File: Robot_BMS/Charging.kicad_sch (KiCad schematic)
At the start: 33 parts, among them Q16 2N7002, Q17 2N7002, Q18 2N7002, U10 MCP73833-xxx-MF, U11 MCP73833-xxx-MF, U12 MCP73833-xxx-MF

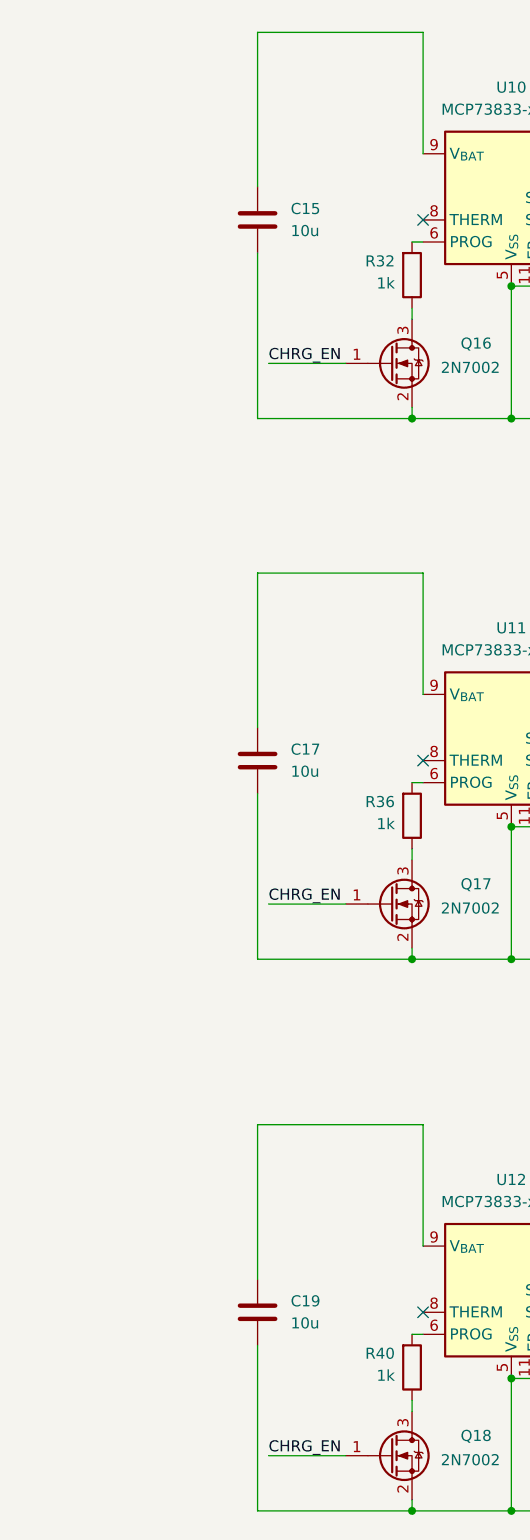
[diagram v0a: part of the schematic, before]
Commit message: cleaning up hierarchical schematics
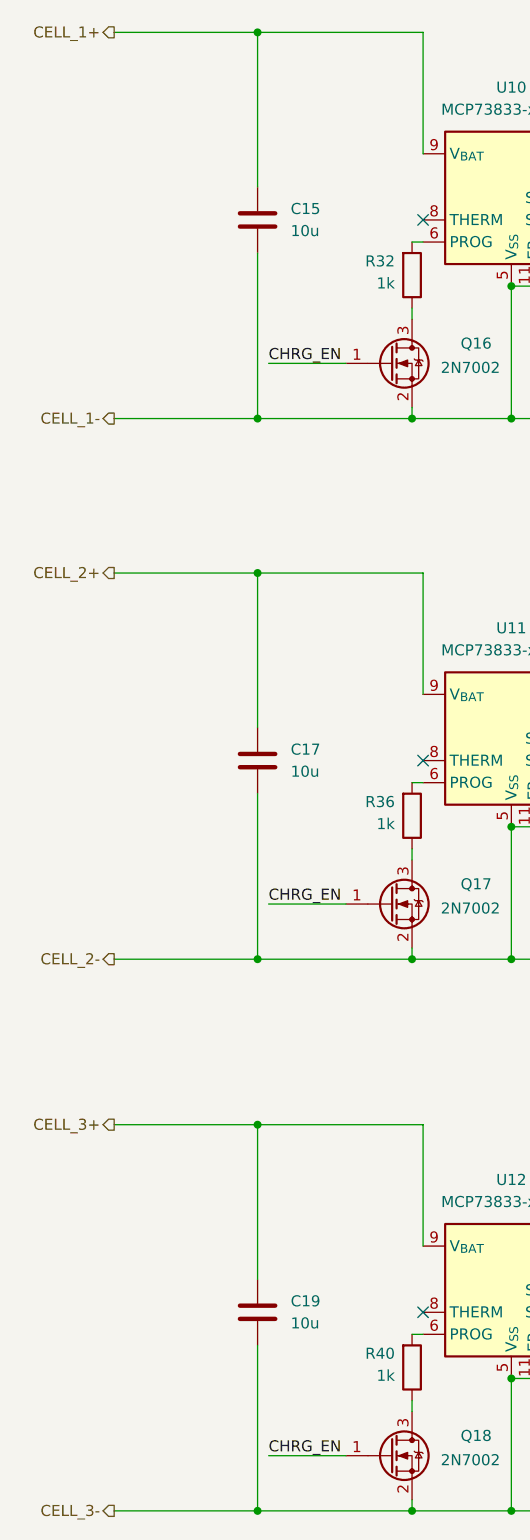
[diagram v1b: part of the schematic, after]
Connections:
- net CELL_2+: now reaches C17.1, U11.10 (V_{BAT}), U11.9 (V_{BAT})
- net CELL_2-: now reaches C17.2, C18.2, Q17.2 (S), U11.11 (EP), U11.5 (V_{SS})
- net CELL_3-: now reaches C19.2, C20.2, Q18.2 (S), U12.11 (EP), U12.5 (V_{SS})
- net CELL_3+: now reaches C19.1, U12.10 (V_{BAT}), U12.9 (V_{BAT})
- net CELL_1-: now reaches C15.2, C16.2, Q16.2 (S), U10.11 (EP), U10.5 (V_{SS})
- net CELL_1+: now reaches C15.1, U10.10 (V_{BAT}), U10.9 (V_{BAT})
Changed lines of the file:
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@@
+	)
+	(junction
+		(at 41.91 20.32)
+		(diameter 0)
+		(color 0 0 0 0)
+	)
+	(junction
+		(at 41.91 127)
+		(diameter 0)
+		(color 0 0 0 0)
 	)
 	(junction
@@
 	)
 	(junction
+		(at 41.91 64.77)
+		(diameter 0)
+		(color 0 0 0 0)
+	)
+	(junction
+		(at 41.91 146.05)
+		(diameter 0)
+		(color 0 0 0 0)
+	)
+	(junction
 		(at 153.67 19.05)
 		(diameter 0)
@@
 	)
 	(junction
+		(at 41.91 190.5)
+		(diameter 0)
+		(color 0 0 0 0)
+	)
+	(junction
 		(at 71.12 175.26)
 		(diameter 0)
@@
 	(junction
 		(at 153.67 144.78)
+		(diameter 0)
+		(color 0 0 0 0)
+	)
+	(junction
+		(at 41.91 82.55)
 		(diameter 0)
 		(color 0 0 0 0)
@@
 	(wire
 		(pts
+			(xy 25.4 127) (xy 41.91 127)
+		)
+		(stroke
+			(width 0)
+			(type default)
+		)
+	)
+	(wire
+		(pts
 			(xy 163.83 81.28) (xy 163.83 96.52)
 		)
@@
 	(wire
 		(pts
+			(xy 25.4 20.32) (xy 41.91 20.32)
+		)
+		(stroke
+			(width 0)
+			(type default)
+		)
+	)
+	(wire
+		(pts
 			(xy 115.57 34.29) (xy 153.67 34.29)
 		)
@@
 	(wire
 		(pts
+			(xy 25.4 64.77) (xy 41.91 64.77)
+		)
+		(stroke
+			(width 0)
+			(type default)
+		)
+	)
+	(wire
+		(pts
 			(xy 96.52 167.64) (xy 109.22 167.64)
 		)
@@
 	(wire
 		(pts
+			(xy 25.4 146.05) (xy 41.91 146.05)
+		)
+		(stroke
+			(width 0)
+			(type default)
+		)
+	)
+	(wire
+		(pts
 			(xy 99.06 49.53) (xy 115.57 49.53)
 		)
@@
 	(wire
 		(pts
+			(xy 25.4 82.55) (xy 41.91 82.55)
+		)
+		(stroke
+			(width 0)
+			(type default)
+		)
+	)
+	(wire
+		(pts
 			(xy 153.67 144.78) (xy 109.22 144.78)
 		)
@@
 		(pts
 			(xy 41.91 146.05) (xy 41.91 163.83)
+		)
+		(stroke
+			(width 0)
+			(type default)
+		)
+	)
+	(wire
+		(pts
+			(xy 25.4 190.5) (xy 41.91 190.5)
 		)
 		(stroke
@@
 		)
 	)
+	(hierarchical_label "CELL_3+"
+		(shape output)
+		(at 25.4 146.05 180)
+		(effects
+			(font
+				(size 1.27 1.27)
+			)
+			(justify right)
+		)
+	)
+	(hierarchical_label "CELL_2-"
+		(shape output)
+		(at 25.4 127 180)
+		(effects
+			(font
+				(size 1.27 1.27)
+			)
+			(justify right)
+		)
+	)
+	(hierarchical_label "CELL_3-"
+		(shape output)
+		(at 25.4 190.5 180)
+		(effects
+			(font
+				(size 1.27 1.27)
+			)
+			(justify right)
+		)
+	)
+	(hierarchical_label "CELL_2+"
+		(shape output)
+		(at 25.4 82.55 180)
+		(effects
+			(font
+				(size 1.27 1.27)
+			)
+			(justify right)
+		)
+	)
+	(hierarchical_label "CELL_1+"
+		(shape output)
+		(at 25.4 20.32 180)
+		(effects
+			(font
+				(size 1.27 1.27)
+			)
+			(justify right)
+		)
+	)
+	(hierarchical_label "CELL_1-"
+		(shape output)
+		(at 25.4 64.77 180)
+		(effects
+			(font
+				(size 1.27 1.27)
+			)
+			(justify right)
+		)
+	)

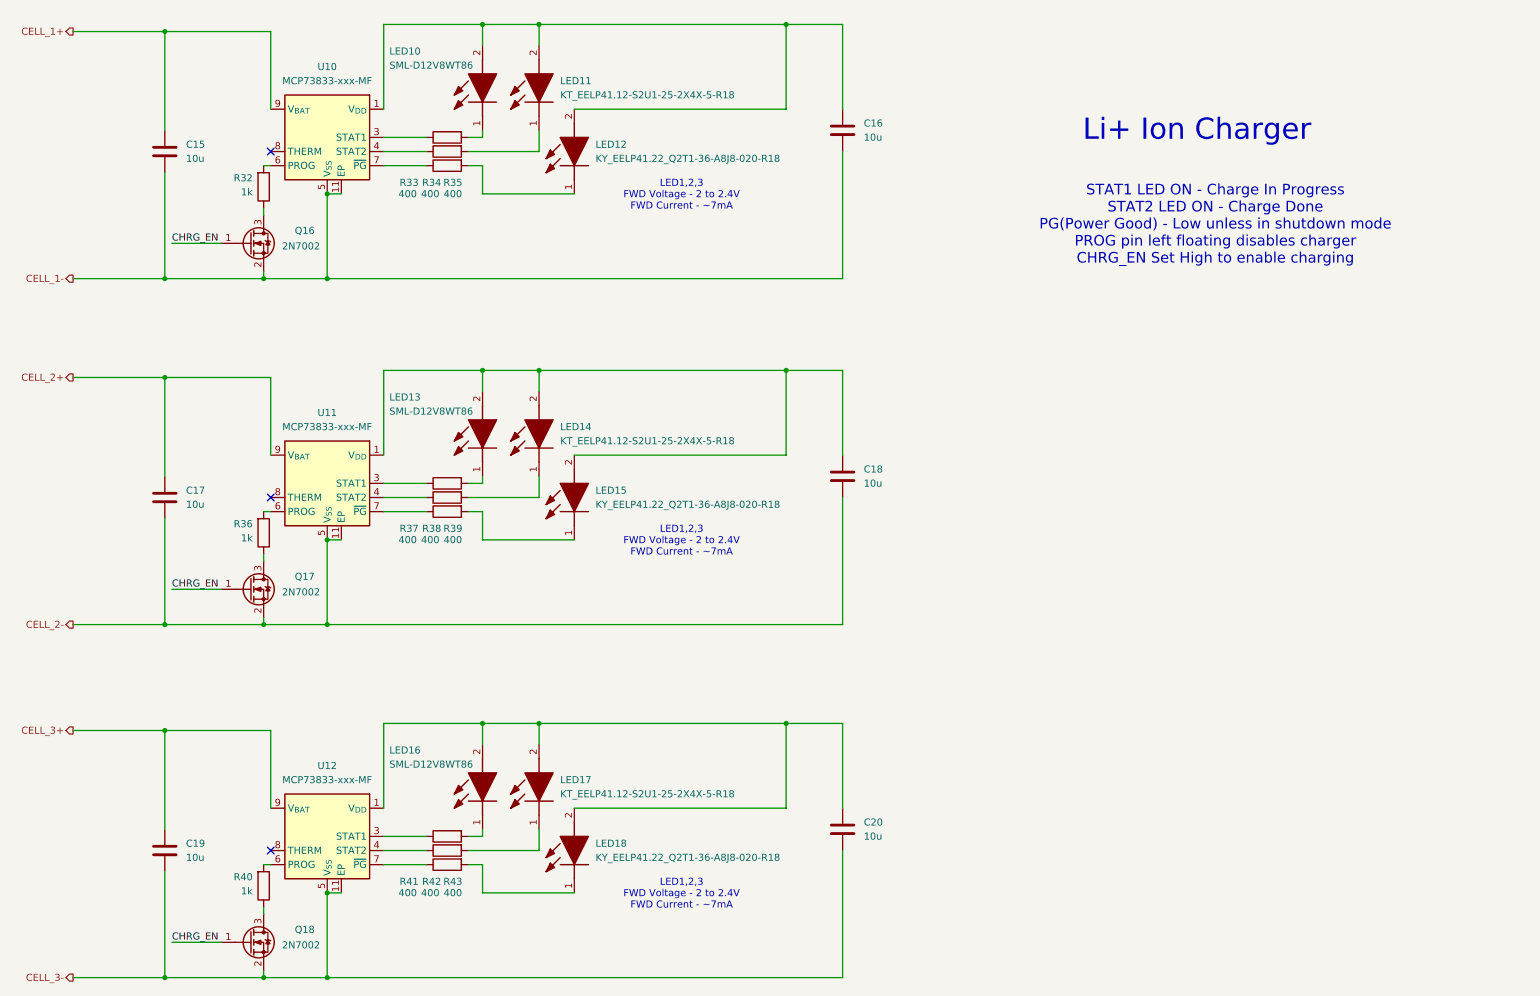
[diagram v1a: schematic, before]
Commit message: DC power supply added via dc Barrel jack
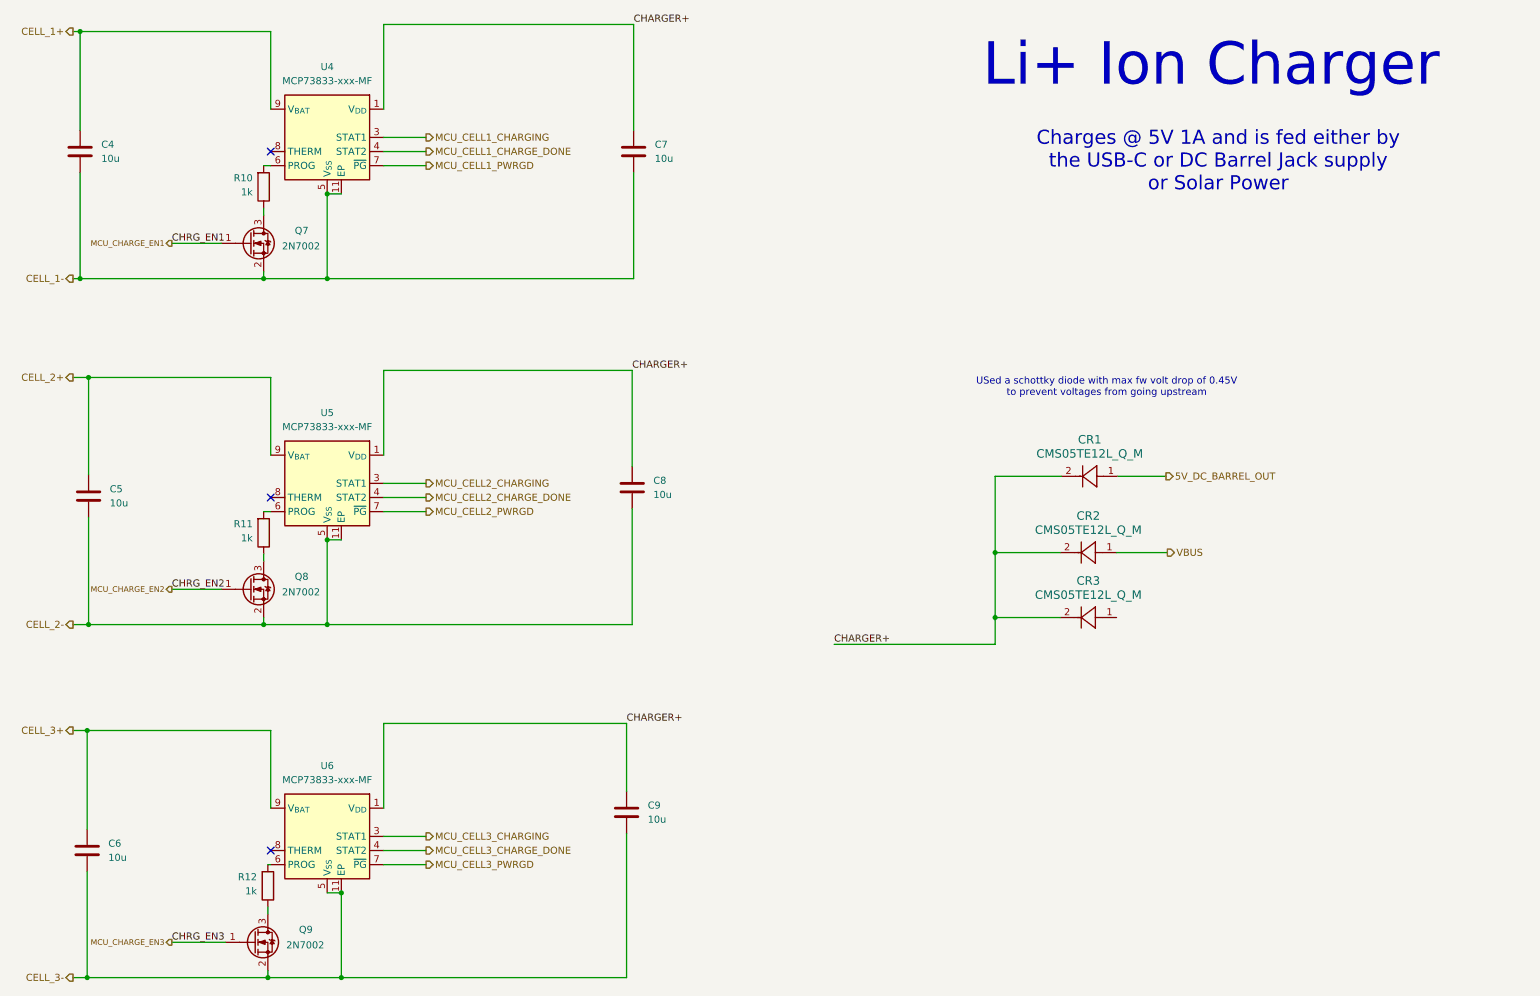
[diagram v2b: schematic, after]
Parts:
- removed LED10, LED13, LED16: SML-D12V8WT86, SMLD12V8WT86, symbol SML-D12V8WT86:SML-D12V8WT86
- removed LED11, LED14, LED17: KT_EELP41.12-S2U1-25-2X4X-5-R18, KTEELP4112S2U1252X4X5R18, symbol KT EELP41.12-S2U1-25-2X4X-5-R18:KT_EELP41.12-S2U1-25-2X4X-5-R18
- removed LED12, LED15, LED18: KY_EELP41.22_Q2T1-36-A8J8-020-R18, KYEELP4122Q2T136A8J8020R18, symbol KY EELP41.22 Q2T1-36-A8J8-020-R18:KY_EELP41.22_Q2T1-36-A8J8-020-R18
- removed R33, R34, R35, R37, R38, R39, R41, R42, R43: 400, symbol Device:R
- added CR1, CR2, CR3: CMS05TE12L_Q_M, M-FLAT_TOS, symbol Toshiba schottky diode:CMS05TE12L_Q_M
- renumbered C15 to C4, C17 to C5, C19 to C6, C16 to C7, C18 to C8, C20 to C9, Q16 to Q7, Q17 to Q8, Q18 to Q9, R32 to R10, R36 to R11, R40 to R12, U10 to U4, U11 to U5, U12 to U6
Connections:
- net MCU_CELL1_CHARGE_DONE: now reaches U4.4 (STAT2)
- net MCU_CELL3_CHARGING: now reaches U6.3 (STAT1)
- net MCU_CELL1_CHARGING: now reaches U4.3 (STAT1)
- net CHARGER+: now reaches C8.1, U5.1 (V_{DD}), U5.2 (V_{DD})
- net CHARGER+: now also C7.1, C9.1, U4.1 (V_{DD}), U4.2 (V_{DD}), U6.1 (V_{DD}), U6.2 (V_{DD}), CR1.2, CR2.2, CR3.2
- net MCU_CELL2_CHARGING: now reaches U5.3 (STAT1)
- net MCU_CELL2_CHARGE_DONE: now reaches U5.4 (STAT2)
- net MCU_CELL2_PWRGD: now reaches U5.7 (~{PG})
- net MCU_CELL1_PWRGD: now reaches U4.7 (~{PG})
- net MCU_CELL3_CHARGE_DONE: now reaches U6.4 (STAT2)
- net MCU_CELL3_PWRGD: now reaches U6.7 (~{PG})
- removed net CHRG_EN: Q7.1 (G), Q8.1 (G), Q9.1 (G)
- new net 5V_DC_BARREL_OUT: CR1.1
- new net MCU_CHARGE_EN1: Q7.1 (G)
- new net MCU_CHARGE_EN2: Q8.1 (G)
- new net MCU_CHARGE_EN3: Q9.1 (G)
- new net VBUS: CR2.1
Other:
- note added: "Charges @ 5V 1A and is fed either by the USB-C or DC Barrel Jack supply or Solar Power"
- note added: "USed a schottky diode with max fw volt drop of 0.45V to prevent voltages from going upstream"
- note removed: "LED1,2,3 FWD Voltage - 2 to 2.4V FWD Current - ~7mA"
- note removed: "STAT1 LED ON - Charge In Progress STAT2 LED ON - Charge Done PG(Power Good) - Low unless in shutdown mode PROG pin left floating disables charger CHRG_EN Set High to enable charging"
- moved on the sheet: C4, C5, C6, C7, C8, C9, Q9, R12

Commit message: implementing sepic converter for Solar power input
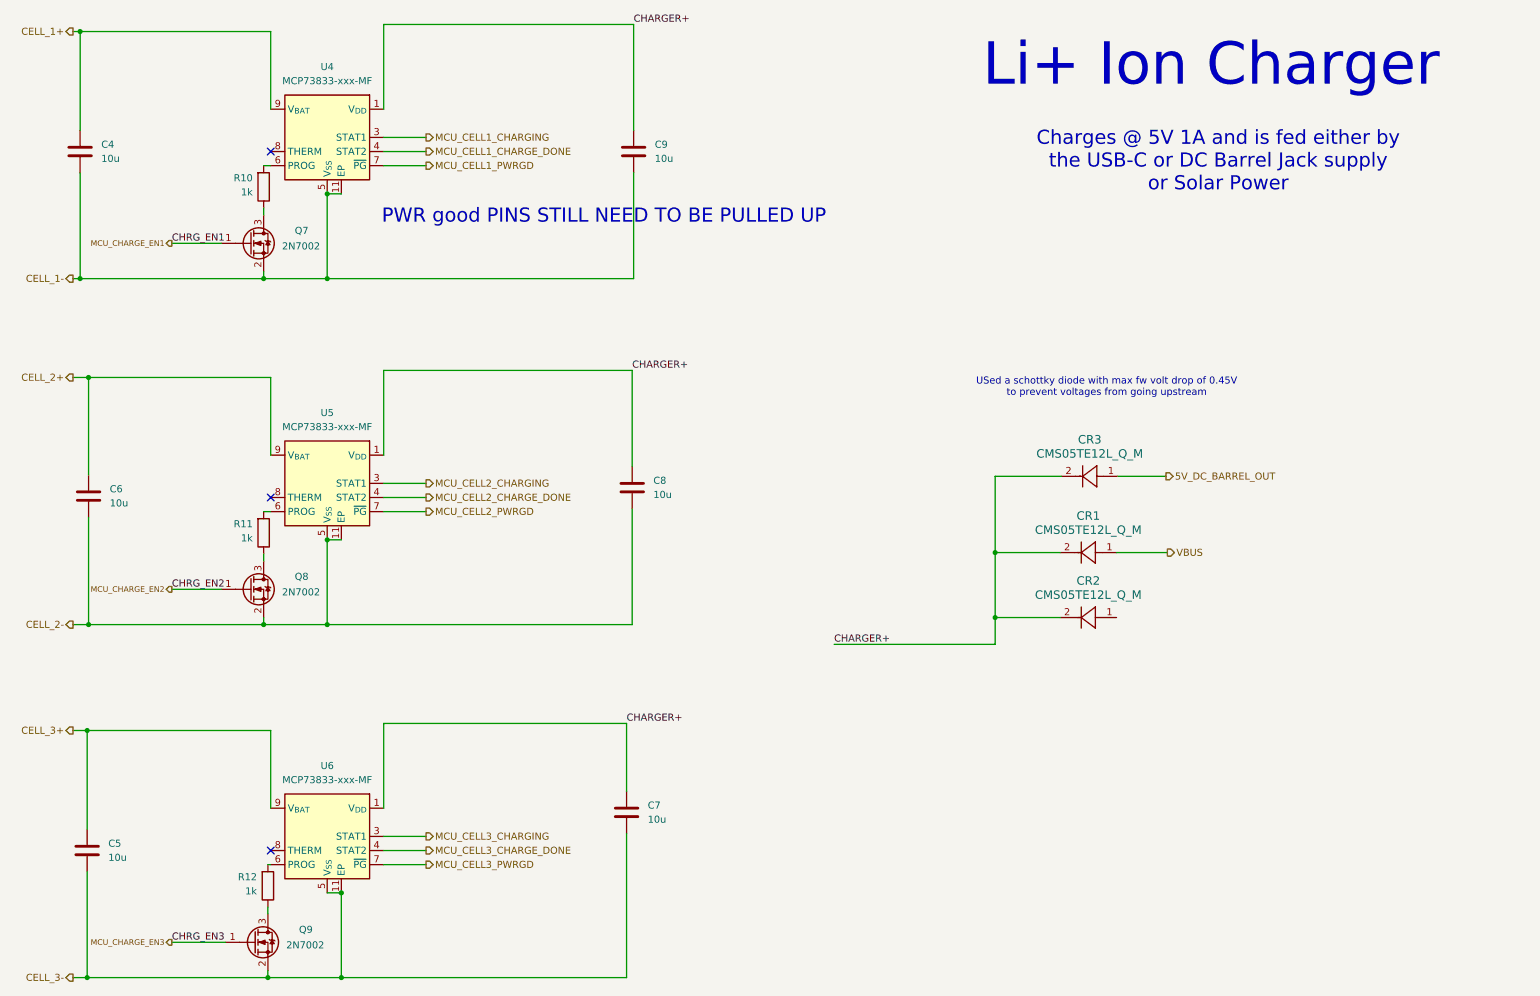
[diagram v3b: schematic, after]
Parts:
- renumbered C6 to C5, C5 to C6, C9 to C7, C7 to C9, CR2 to CR1, CR3 to CR2, CR1 to CR3
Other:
- note added: "PWR good PINS STILL NEED TO BE PULLED UP"
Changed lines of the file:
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@@
+		)
+	)
+	(text "PWR good PINS STILL NEED TO BE PULLED UP"
+		(exclude_from_sim no)
+		(at 120.904 53.594 0)
+		(effects
+			(font
+				(size 2.54 2.54)
+			)
 		)
 	)
@@
 		(dnp no)
 		(fields_autoplaced yes)
-		(property "Reference" "C5"
+		(property "Reference" "C6"
 			(at 32.004 102.6159 0)
 			(effects
@@
 			(project "Robot_BMS"
 				(path "/72551b1c-3d40-4199-8911-e5b015f4abec/c0de399f-bcaa-40ff-9d4f-05779018e40a"
-					(reference "C5")
+					(reference "C6")
 					(unit 1)
 				)
@@
 		(dnp no)
 		(fields_autoplaced yes)
-		(property "Reference" "CR3"
+		(property "Reference" "CR2"
 			(at 208.026 119.126 0)
 			(effects
@@
 			(project "Robot_BMS"
 				(path "/72551b1c-3d40-4199-8911-e5b015f4abec/c0de399f-bcaa-40ff-9d4f-05779018e40a"
-					(reference "CR3")
+					(reference "CR2")
 					(unit 1)
 				)
@@
 		(dnp no)
 		(fields_autoplaced yes)
-		(property "Reference" "C9"
+		(property "Reference" "C7"
 			(at 128.778 159.5119 0)
 			(effects
@@
 			(project "Robot_BMS"
 				(path "/72551b1c-3d40-4199-8911-e5b015f4abec/c0de399f-bcaa-40ff-9d4f-05779018e40a"
-					(reference "C9")
+					(reference "C7")
 					(unit 1)
 				)
@@
 		(dnp no)
 		(fields_autoplaced yes)
-		(property "Reference" "CR1"
+		(property "Reference" "CR3"
 			(at 208.28 93.726 0)
 			(effects
@@
 			(project ""
 				(path "/72551b1c-3d40-4199-8911-e5b015f4abec/c0de399f-bcaa-40ff-9d4f-05779018e40a"
-					(reference "CR1")
+					(reference "CR3")
 					(unit 1)
 				)
@@
 		(dnp no)
 		(fields_autoplaced yes)
-		(property "Reference" "C6"
+		(property "Reference" "C5"
 			(at 31.75 166.3699 0)
 			(effects
@@
 			(project "Robot_BMS"
 				(path "/72551b1c-3d40-4199-8911-e5b015f4abec/c0de399f-bcaa-40ff-9d4f-05779018e40a"
-					(reference "C6")
+					(reference "C5")
 					(unit 1)
 				)
@@
 		(dnp no)
 		(fields_autoplaced yes)
-		(property "Reference" "C7"
+		(property "Reference" "C9"
 			(at 130.048 40.6399 0)
 			(effects
@@
 			(project "Robot_BMS"
 				(path "/72551b1c-3d40-4199-8911-e5b015f4abec/c0de399f-bcaa-40ff-9d4f-05779018e40a"
-					(reference "C7")
+					(reference "C9")
 					(unit 1)
 				)
@@
 		(dnp no)
 		(fields_autoplaced yes)
-		(property "Reference" "CR2"
+		(property "Reference" "CR1"
 			(at 208.026 107.442 0)
 			(effects
@@
 			(project "Robot_BMS"
 				(path "/72551b1c-3d40-4199-8911-e5b015f4abec/c0de399f-bcaa-40ff-9d4f-05779018e40a"
-					(reference "CR2")
-					(unit 1)
-				)
+					(reference "CR1")
+					(unit 1)
+				)
